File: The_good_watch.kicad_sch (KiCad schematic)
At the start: 50 parts, among them IC1 DW01A, J1 Main, J2 USB_C_Receptacle_USB2.0, J3 PROG, J4 Screen, J5 Button, J6 Conn_02x07_Counter_Clockwise, M1 Motor_DC, Q1 FS8205A, Q2 LP0404N3T5G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

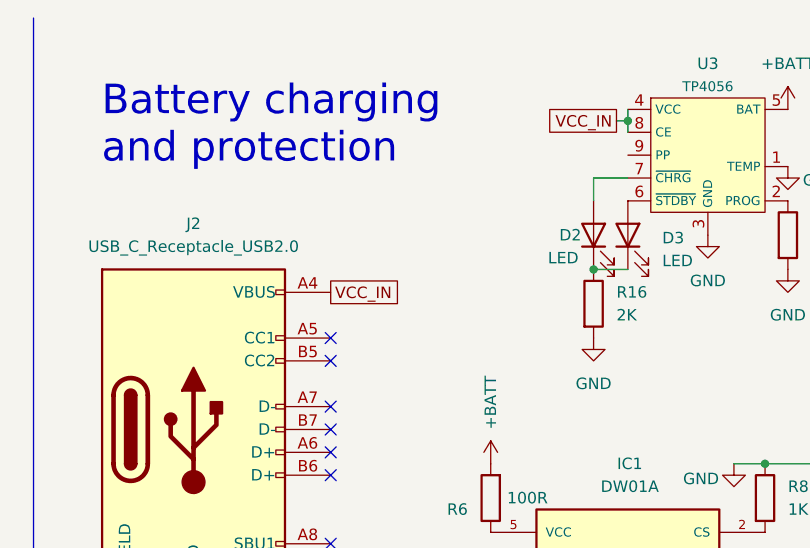
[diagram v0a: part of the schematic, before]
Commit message: Added schottky diode for reverse voltage protection
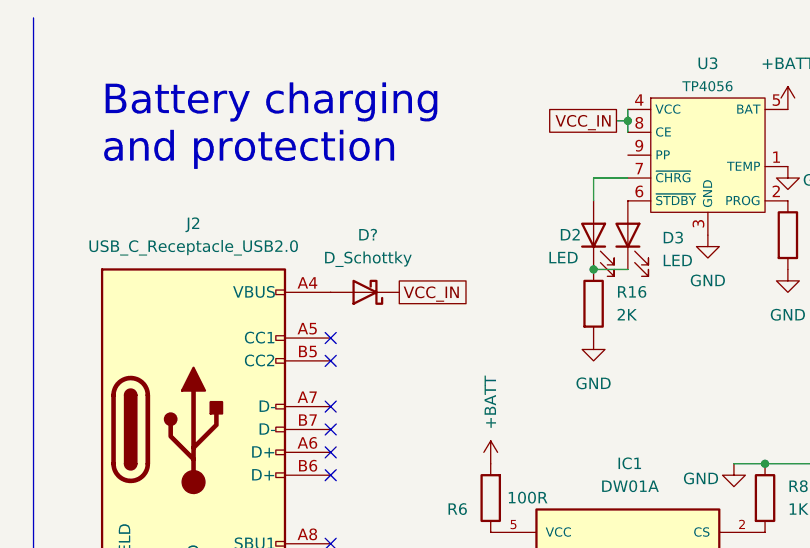
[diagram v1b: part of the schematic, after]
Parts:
- added D?: D_Schottky, symbol Device:D_Schottky
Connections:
- net VCC_IN: now also D?.1 (K); no longer J2.A4 (VBUS), J2.A9 (VBUS), J2.B4 (VBUS), J2.B9 (VBUS)
- new net: D?.2 (A), J2.A4 (VBUS), J2.A9 (VBUS), J2.B4 (VBUS), J2.B9 (VBUS)
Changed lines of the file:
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@@
     (effects (font (size 1.27 1.27)) (justify left bottom))
   )
-  (global_label "VCC_IN" (shape passive) (at 209.55 41.91 0) (fields_autoplaced)
-    (effects (font (size 1.27 1.27)) (justify left))
-    (property "Intersheet References" "${INTERSHEET_REFS}" (id 0) (at 218.4945 41.8306 0)
+  (global_label "VCC_IN" (shape passive) (at 217.17 41.91 0) (fields_autoplaced)
+    (effects (font (size 1.27 1.27)) (justify left))
+    (property "Intersheet References" "${INTERSHEET_REFS}" (id 0) (at 226.1145 41.8306 0)
       (effects (font (size 1.27 1.27)) (justify left) hide)
     )
@@
     (pin "6")
   )
+  (symbol (lib_id "Device:D_Schottky") (at 213.36 41.91 180) (unit 1)
+    (in_bom yes) (on_board yes) (fields_autoplaced)
+    (property "Reference" "D?" (id 0) (at 213.6775 35.56 0))
+    (property "Value" "D_Schottky" (id 1) (at 213.6775 38.1 0))
+    (property "Footprint" "" (id 2) (at 213.36 41.91 0)
+      (effects (font (size 1.27 1.27)) hide)
+    )
+    (property "Datasheet" "~" (id 3) (at 213.36 41.91 0)
+      (effects (font (size 1.27 1.27)) hide)
+    )
+    (pin "1")
+    (pin "2")
+  )
   (symbol (lib_id "power:+3.3V") (at 17.6784 44.4246 0) (unit 1)
     (in_bom yes) (on_board yes)
@@
       (reference "D4") (unit 1) (value "D_Schottky") (footprint "Diode_SMD:D_0603_1608Metric")
     )
+    (path "/9d054268-850d-4bb1-849a-a7f37dccd552"
+      (reference "D?") (unit 1) (value "D_Schottky") (footprint "")
+    )
     (path "/94868651-0943-45d2-80cb-19057554eb97"

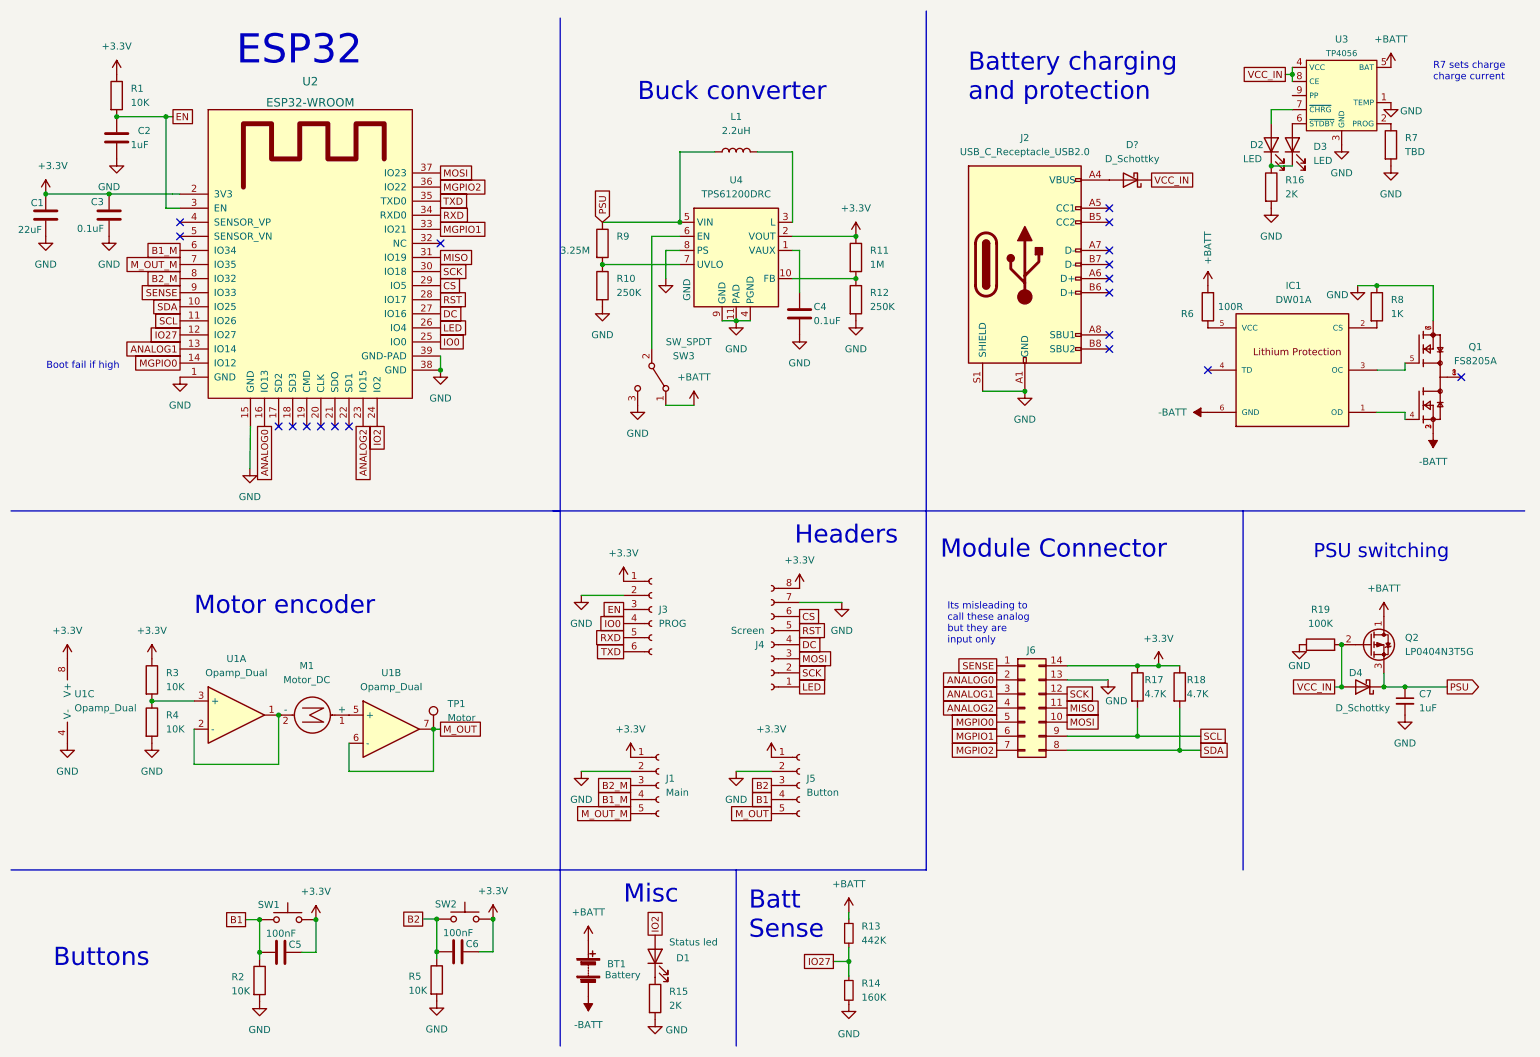
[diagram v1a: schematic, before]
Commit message: Added diode protection on usb pwr in and redid layout
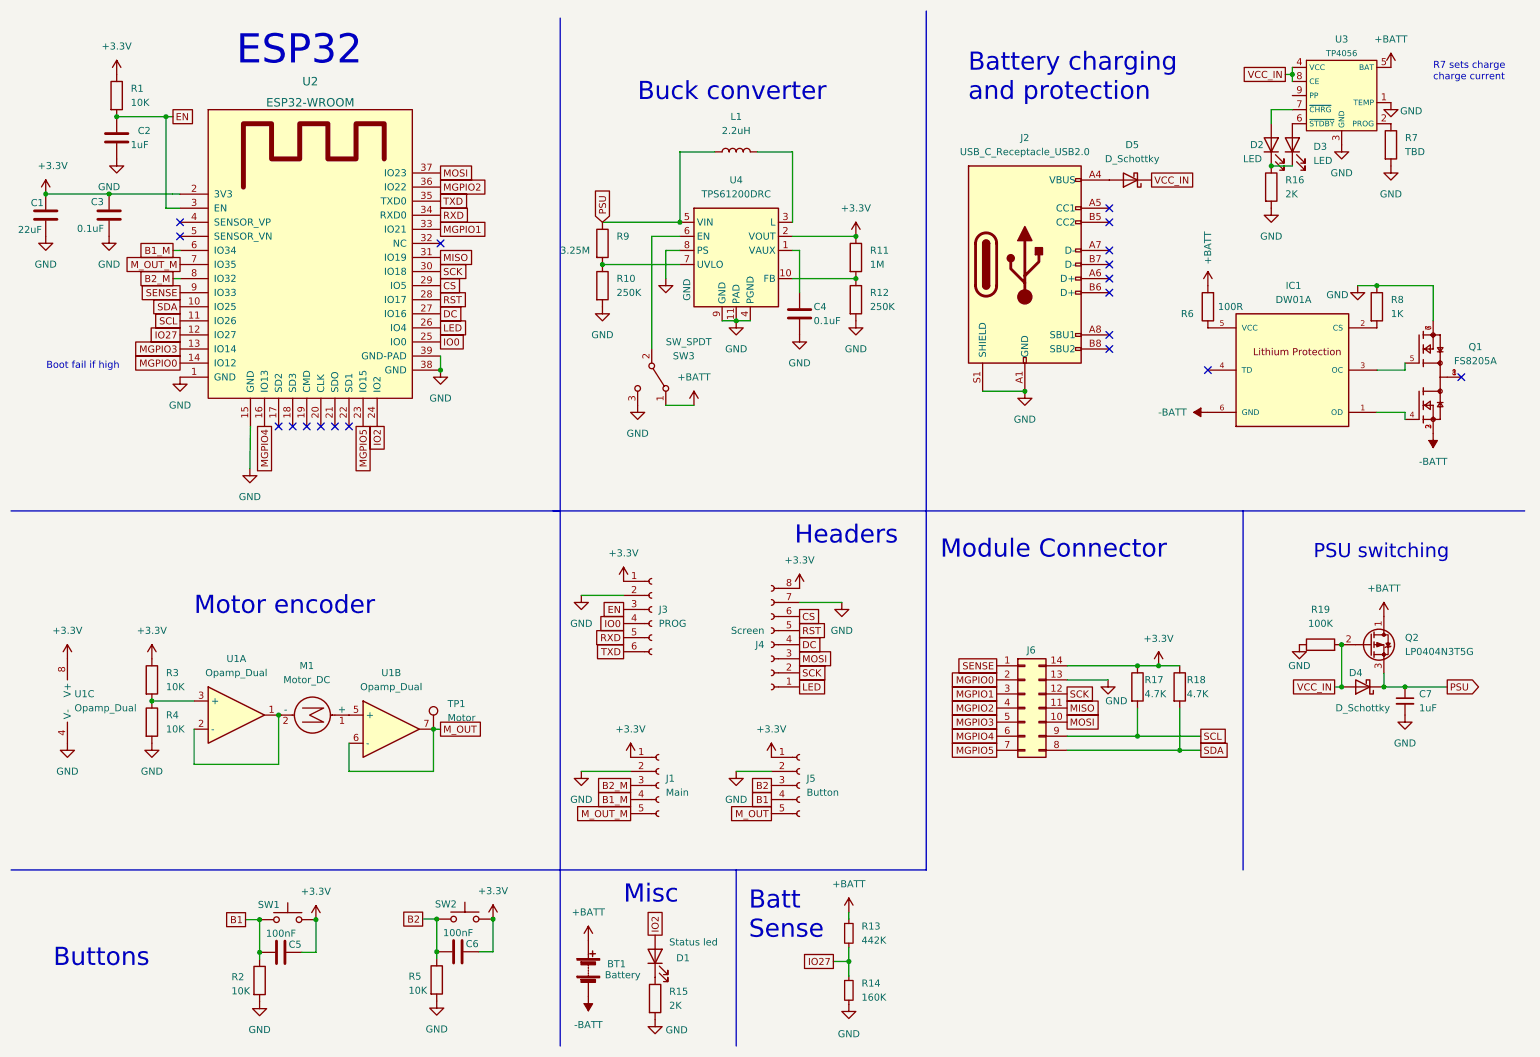
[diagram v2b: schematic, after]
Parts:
- D5: renamed from D?; footprint (none) -> Diode_SMD:D_0603_1608Metric
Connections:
- net MGPIO0: now also J6.2 (Pin_2); no longer J6.5 (Pin_5)
- net MGPIO1: now also J6.3 (Pin_3); no longer J6.6 (Pin_6)
- net MGPIO2: now also J6.4 (Pin_4); no longer J6.7 (Pin_7)
- net ANALOG0 renamed MGPIO4
- net MGPIO4: now also J6.6 (Pin_6); no longer J6.2 (Pin_2)
- net ANALOG1 renamed MGPIO3
- net MGPIO3: now also J6.5 (Pin_5); no longer J6.3 (Pin_3)
- net ANALOG2 renamed MGPIO5
- net MGPIO5: now also J6.7 (Pin_7); no longer J6.4 (Pin_4)
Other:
- note removed: "Its misleading to call these analog but they are input only"
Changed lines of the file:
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@@
   (no_connect (at 88.9 53.34))
   (no_connect (at 227.33 76.2))
+  (wire (pts (xy 40.64 59.69) (xy 41.91 59.69))
+    (stroke (width 0) (type default) (color 0 0 0 0))
+  )
   (wire (pts (xy 44.45 140.97) (xy 44.45 147.32))
     (stroke (width 0) (type default) (color 0 0 0 0))
@@
     (stroke (width 0) (type default) (color 0 0 0 0))
   )
+  (wire (pts (xy 40.64 54.61) (xy 41.91 54.61))
+    (stroke (width 0) (type default) (color 0 0 0 0))
+  )
   (wire (pts (xy 87.63 148.59) (xy 87.63 140.97))
     (stroke (width 0) (type default) (color 0 0 0 0))
@@
     (effects (font (size 3.27 3.27)) (justify left bottom))
   )
-  (text "Its misleading to\ncall these analog\nbut they are\ninput only"
-    (at 180.34 125.73 0)
-    (effects (font (size 1.27 1.27)) (justify left bottom))
-  )
   (global_label "VCC_IN" (shape passive) (at 217.17 41.91 0) (fields_autoplaced)
     (effects (font (size 1.27 1.27)) (justify left))
@@
     )
   )
-  (global_label "ANALOG1" (shape passive) (at 41.91 72.39 180) (fields_autoplaced)
+  (global_label "MGPIO3" (shape passive) (at 41.91 72.39 180) (fields_autoplaced)
     (effects (font (size 1.27 1.27)) (justify right))
-    (property "Intersheet References" "${INTERSHEET_REFS}" (id 0) (at 31.1512 72.3106 0)
+    (property "Intersheet References" "${INTERSHEET_REFS}" (id 0) (at 32.3607 72.3106 0)
       (effects (font (size 1.27 1.27)) (justify right) hide)
     )
   )
-  (global_label "ANALOG2" (shape passive) (at 74.93 86.36 270) (fields_autoplaced)
+  (global_label "MGPIO5" (shape passive) (at 74.93 86.36 270) (fields_autoplaced)
     (effects (font (size 1.27 1.27)) (justify right))
-    (property "Intersheet References" "${INTERSHEET_REFS}" (id 0) (at 74.8506 97.1188 90)
+    (property "Intersheet References" "${INTERSHEET_REFS}" (id 0) (at 74.8506 95.9093 90)
       (effects (font (size 1.27 1.27)) (justify right) hide)
     )
@@
     )
   )
-  (global_label "B2_M" (shape passive) (at 41.91 59.69 180) (fields_autoplaced)
+  (global_label "B2_M" (shape passive) (at 40.64 59.69 180) (fields_autoplaced)
     (effects (font (size 1.27 1.27)) (justify right))
-    (property "Intersheet References" "${INTERSHEET_REFS}" (id 0) (at 34.5983 59.6106 0)
+    (property "Intersheet References" "${INTERSHEET_REFS}" (id 0) (at 33.3283 59.6106 0)
       (effects (font (size 1.27 1.27)) (justify right) hide)
     )
@@
     )
   )
-  (global_label "ANALOG1" (shape passive) (at 189.23 134.62 180) (fields_autoplaced)
+  (global_label "MGPIO1" (shape passive) (at 189.23 134.62 180) (fields_autoplaced)
     (effects (font (size 1.27 1.27)) (justify right))
-    (property "Intersheet References" "${INTERSHEET_REFS}" (id 0) (at 178.4712 134.5406 0)
+    (property "Intersheet References" "${INTERSHEET_REFS}" (id 0) (at 179.6807 134.5406 0)
       (effects (font (size 1.27 1.27)) (justify right) hide)
     )
   )
-  (global_label "MGPIO0" (shape passive) (at 189.23 139.7 180) (fields_autoplaced)
+  (global_label "MGPIO3" (shape passive) (at 189.23 139.7 180) (fields_autoplaced)
     (effects (font (size 1.27 1.27)) (justify right))
     (property "Intersheet References" "${INTERSHEET_REFS}" (id 0) (at 179.6807 139.6206 0)
@@
     )
   )
-  (global_label "B1_M" (shape passive) (at 41.91 54.61 180) (fields_autoplaced)
+  (global_label "B1_M" (shape passive) (at 40.64 54.61 180) (fields_autoplaced)
     (effects (font (size 1.27 1.27)) (justify right))
-    (property "Intersheet References" "${INTERSHEET_REFS}" (id 0) (at 34.5983 54.5306 0)
+    (property "Intersheet References" "${INTERSHEET_REFS}" (id 0) (at 33.3283 54.5306 0)
       (effects (font (size 1.27 1.27)) (justify right) hide)
     )
@@
     )
   )
-  (global_label "ANALOG2" (shape passive) (at 189.23 137.16 180) (fields_autoplaced)
+  (global_label "MGPIO2" (shape passive) (at 189.23 137.16 180) (fields_autoplaced)
     (effects (font (size 1.27 1.27)) (justify right))
-    (property "Intersheet References" "${INTERSHEET_REFS}" (id 0) (at 178.4712 137.0806 0)
+    (property "Intersheet References" "${INTERSHEET_REFS}" (id 0) (at 179.6807 137.0806 0)
       (effects (font (size 1.27 1.27)) (justify right) hide)
     )
@@
     )
   )
-  (global_label "MGPIO1" (shape passive) (at 189.23 142.24 180) (fields_autoplaced)
+  (global_label "MGPIO4" (shape passive) (at 189.23 142.24 180) (fields_autoplaced)
     (effects (font (size 1.27 1.27)) (justify right))
     (property "Intersheet References" "${INTERSHEET_REFS}" (id 0) (at 179.6807 142.1606 0)
@@
     )
   )
-  (global_label "MGPIO2" (shape passive) (at 189.23 144.78 180) (fields_autoplaced)
+  (global_label "MGPIO5" (shape passive) (at 189.23 144.78 180) (fields_autoplaced)
     (effects (font (size 1.27 1.27)) (justify right))
-    (property "Intersheet References" "${INTERSHEET_REFS}" (id 0) (at 179.6807 144.8594 0)
+    (property "Intersheet References" "${INTERSHEET_REFS}" (id 0) (at 179.6807 144.7006 0)
       (effects (font (size 1.27 1.27)) (justify right) hide)
     )
   )
-  (global_label "ANALOG0" (shape passive) (at 189.23 132.08 180) (fields_autoplaced)
+  (global_label "MGPIO0" (shape passive) (at 189.23 132.08 180) (fields_autoplaced)
     (effects (font (size 1.27 1.27)) (justify right))
-    (property "Intersheet References" "${INTERSHEET_REFS}" (id 0) (at 178.4712 132.0006 0)
+    (property "Intersheet References" "${INTERSHEET_REFS}" (id 0) (at 179.6807 132.0006 0)
       (effects (font (size 1.27 1.27)) (justify right) hide)
     )
@@
     )
   )
-  (global_label "ANALOG0" (shape passive) (at 57.15 86.36 270) (fields_autoplaced)
+  (global_label "MGPIO4" (shape passive) (at 57.15 86.36 270) (fields_autoplaced)
     (effects (font (size 1.27 1.27)) (justify right))
-    (property "Intersheet References" "${INTERSHEET_REFS}" (id 0) (at 57.0706 97.1188 90)
+    (property "Intersheet References" "${INTERSHEET_REFS}" (id 0) (at 57.0706 95.9093 90)
       (effects (font (size 1.27 1.27)) (justify right) hide)
     )
@@
   (symbol (lib_id "Device:D_Schottky") (at 213.36 41.91 180) (unit 1)
     (in_bom yes) (on_board yes) (fields_autoplaced)
-    (property "Reference" "D?" (id 0) (at 213.6775 35.56 0))
+    (property "Reference" "D5" (id 0) (at 213.6775 35.56 0))
     (property "Value" "D_Schottky" (id 1) (at 213.6775 38.1 0))
-    (property "Footprint" "" (id 2) (at 213.36 41.91 0)
+    (property "Footprint" "Diode_SMD:D_0603_1608Metric" (id 2) (at 213.36 41.91 0)
       (effects (font (size 1.27 1.27)) hide)
     )
@@
     )
     (path "/9d054268-850d-4bb1-849a-a7f37dccd552"
-      (reference "D?") (unit 1) (value "D_Schottky") (footprint "")
+      (reference "D5") (unit 1) (value "D_Schottky") (footprint "Diode_SMD:D_0603_1608Metric")
     )
     (path "/94868651-0943-45d2-80cb-19057554eb97"
